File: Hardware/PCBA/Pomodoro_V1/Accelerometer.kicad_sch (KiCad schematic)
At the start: 6 parts, among them U2 LIS2HH12

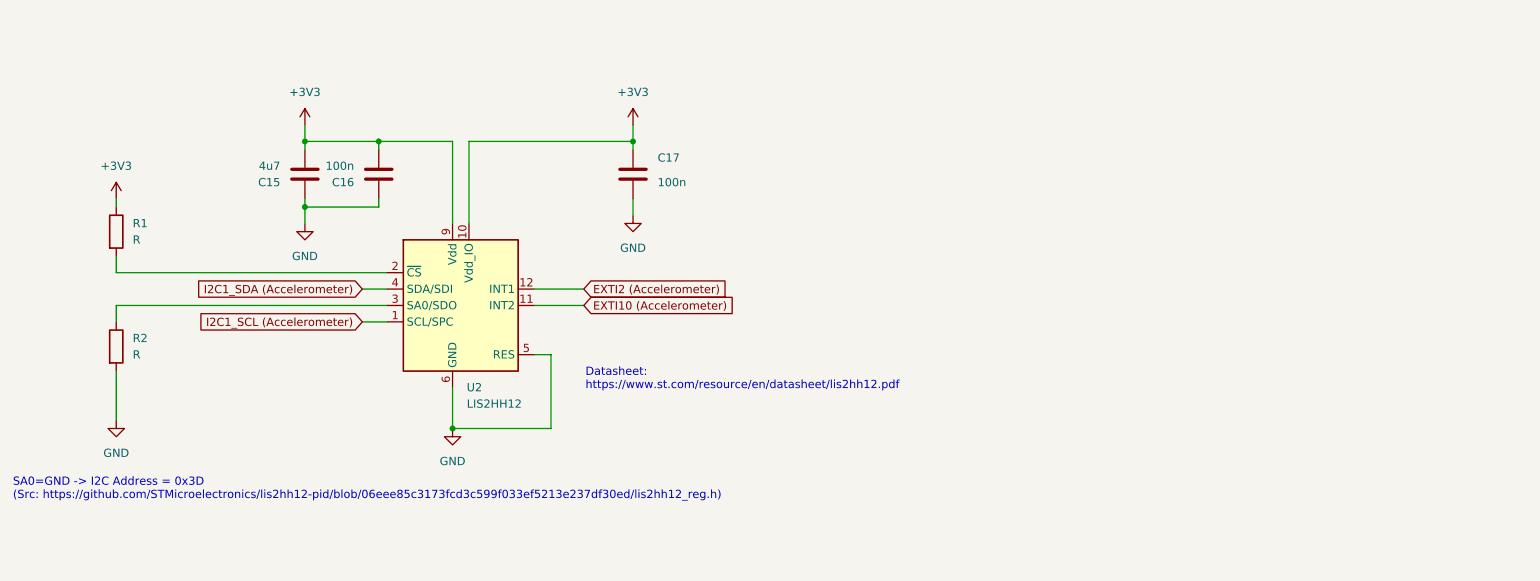
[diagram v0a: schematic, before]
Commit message: Implemented the Rotary encoder, the buttons, the IMU, Added it to the PCB (All the space constraining elements are now placed)
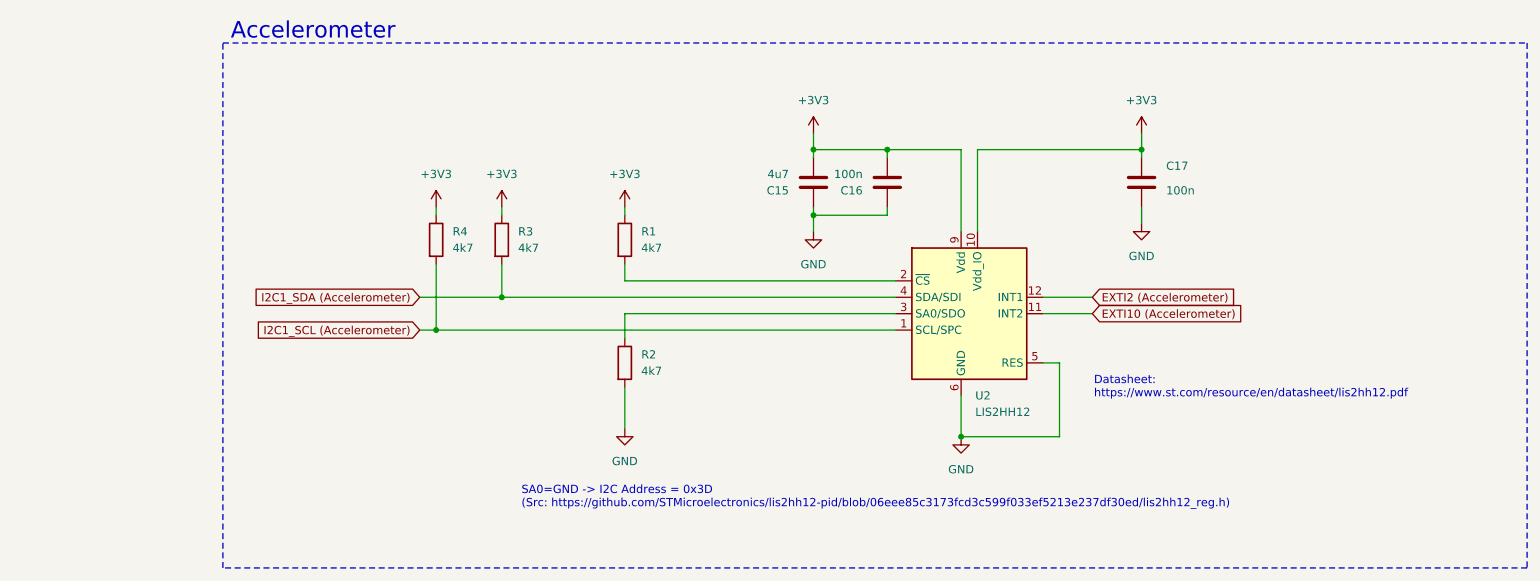
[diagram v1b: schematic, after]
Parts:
- added R3, R4: 4k7, symbol Device:R
- R1, R2: value R -> 4k7
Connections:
- net +3V3: now also R3.1, R4.1
- net I2C1_SCL (Accelerometer): now also R4.2
- net I2C1_SDA (Accelerometer): now also R3.2
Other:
- note added: "Accelerometer"
- moved on the sheet: C15, C16, C17, R1, R2, U2

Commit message: Finalized the schematic, First Draft of the finished Layout
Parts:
- C15, C16, C17: footprint (none) -> Capacitor_SMD:C_0805_2012Metric
- R1, R2, R3, R4: value 4k7 -> 5k1; footprint (none) -> Resistor_SMD:R_0805_2012Metric; Part ID (none) -> CR0805-FX-5101ELF
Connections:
- net +3V3: now also C17.2, R2.1; no longer C17.1, R4.1
- net GND: now also C17.1, R4.2; no longer C17.2, R2.2
- net I2C1_SCL (Accelerometer): now also R3.2; no longer R4.2
- net I2C1_SDA (Accelerometer): now also R2.2; no longer R3.2
- net at U2.3 (SA0/SDO): now also R4.1; no longer R2.1
- net EXTI10 (Accelerometer) renamed EXTI9 (Accelerometer)
- net EXTI2 (Accelerometer) renamed EXTI8 (Accelerometer)

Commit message: Version that was ordered online
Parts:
- C15: value 4u7 -> 1u; Digikey (none) -> https://www.digikey.pt/en/products/detail/nextgen-component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; MPN (none) -> 0805B105K250DC
- C16, C17: Digikey (none) -> https://www.digikey.pt/en/products/detail/yageo/CC0805KRX7R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; MPN (none) -> CC0805KRX7R9BB104
- R1, R2, R3, R4: MPN (none) -> CR0805-FX-5101ELF
- U2: Digikey (none) -> https://www.digikey.pt/en/products/detail/stmicroelectronic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; MPN (none) -> LIS2HH12
